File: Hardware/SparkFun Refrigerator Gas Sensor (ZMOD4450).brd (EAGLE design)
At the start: 25.4 x 25.4 mm, 42 parts, among them J2 QWIIC_RIGHT_ANGLE, J4 QWIIC_RIGHT_ANGLE, U1 ZMOD4450 Refrigeration Gas Se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

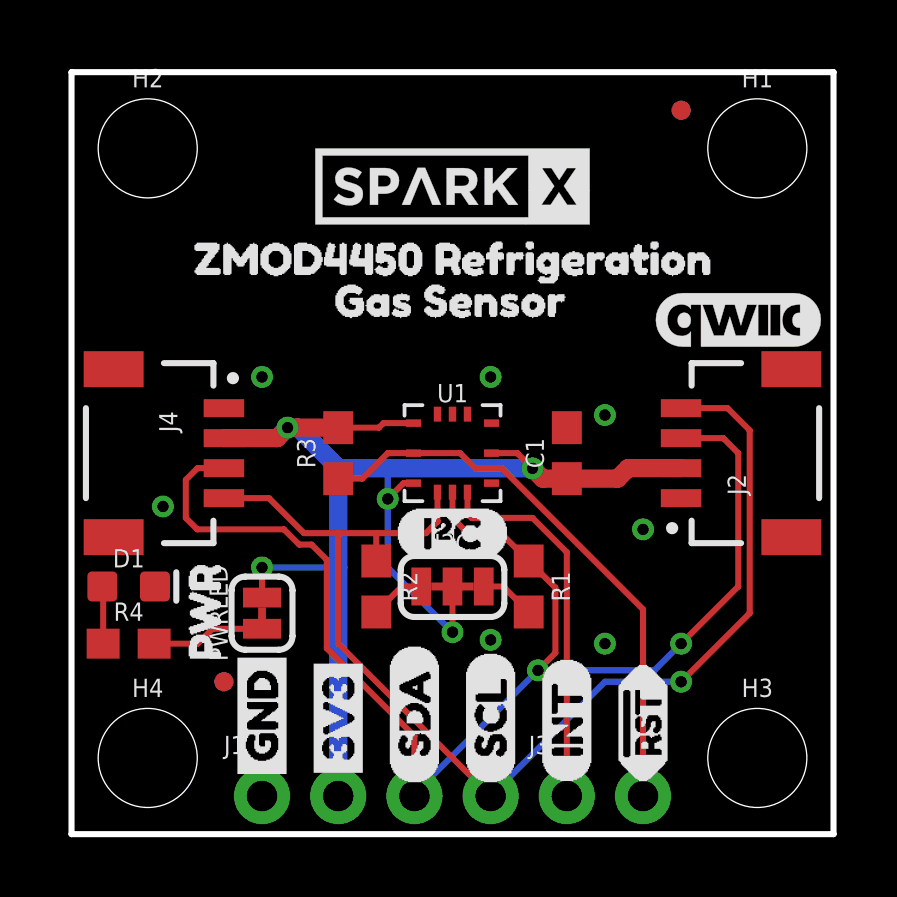
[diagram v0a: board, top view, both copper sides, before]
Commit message: Changing INT silk
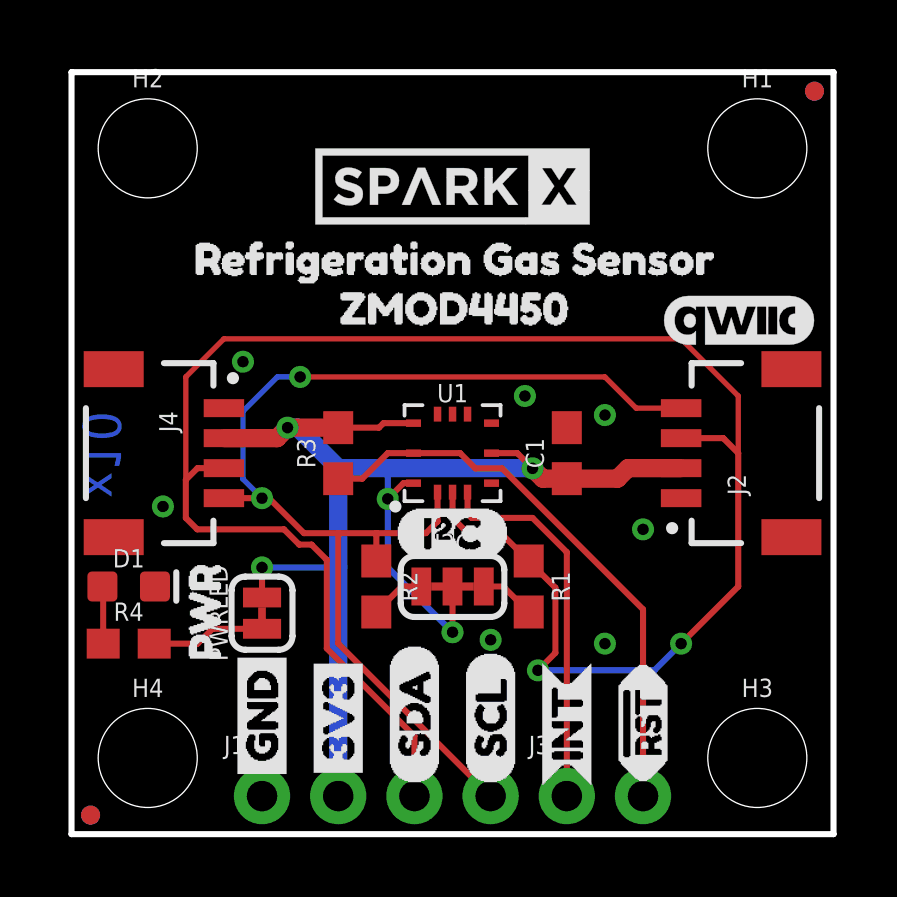
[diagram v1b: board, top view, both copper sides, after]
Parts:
- added LOGO2: QWIIC_LOGO_5MM, SparkFun-Aesthetics:QWIIC_5MM
- added U$20: (no value), buzzard_labels (7):ZMOD44501
- added U$21: (no value), buzzard_labels (8):ADDR#_0X320
- added U$22: (no value), SparkFun-Aesthetics:PRODUCTION_INSTRUCTIONS
- R1, R2, R3: device SparkFun-Resistors:0603@1 -> SparkFun-Resistors:0603
- U$14: device SparkFun-Buzzard:INT -> SparkFun-Buzzard:INT_O
- U$15: device SparkFun-Buzzard:INT -> buzzard_labels (7):REFRIGERATION_GAS_SENSOR0
- U$17: device SparkFun-Aesthetics:QWIIC_5.5MM -> buzzard_labels (7):REFRIGERATION_GAS_SENSOR0
- U$3: device buzzard_labels (5):GAS_SENSOR2 -> buzzard_labels (7):ZMOD44501
- U$4: device buzzard_labels (6):ZMOD4450_REFRIGERATION2 -> SparkFun-Buzzard:INT_O
- moved U$4 22.1 mm to (16.5, 1.52), turned to 90 degrees
- moved U$17 19.2 mm to (3.17, 19.2)
- moved U$15 18.5 mm to (22.5, 19.2), turned to 0 degrees
- moved FD2 6.29 mm to (0.64, 0.64)
- moved FD3 6.29 mm to (0.64, 0.64)
- moved FD1 4.49 mm to (24.8, 24.8)
- moved FD4 4.49 mm to (24.8, 24.8)
- moved U$3 0.28 mm to (8.00, 17.5)
- moved U$14 0.13 mm to (16.5, 1.52), flipped to the bottom
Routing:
- net SDA: track 45.6 -> 64.8 mm
- net SCL: track 40.4 -> 39.2 mm, vias 1 -> 2
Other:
- board text added: "PCB's must be baked before populating"
- board text added: "x10"
